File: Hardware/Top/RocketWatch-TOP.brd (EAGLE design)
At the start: 160 x 100 mm, 0 parts

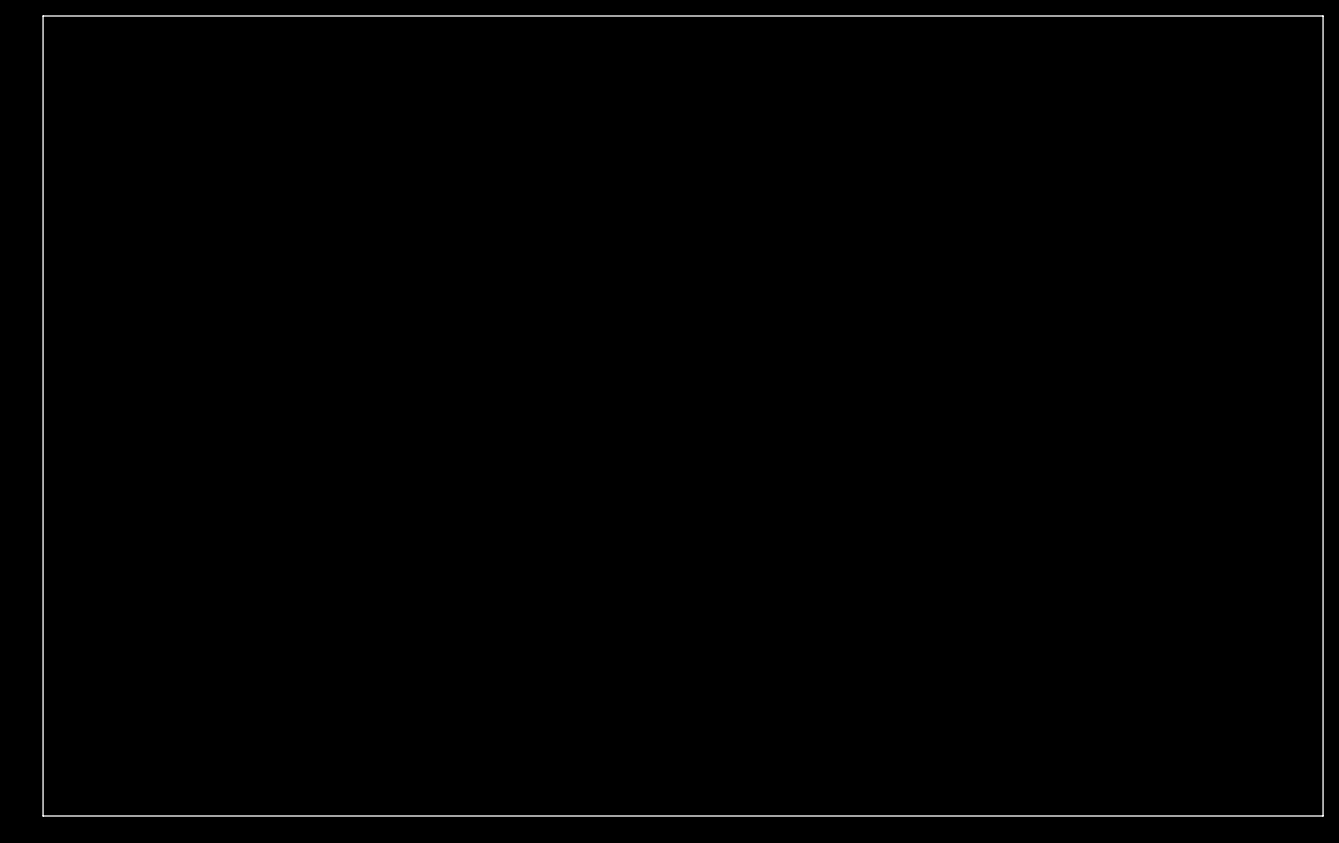
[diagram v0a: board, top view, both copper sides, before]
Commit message: updates to the board and schematic (added microcontroller, power management, OLED, Buttons, and a few other components)
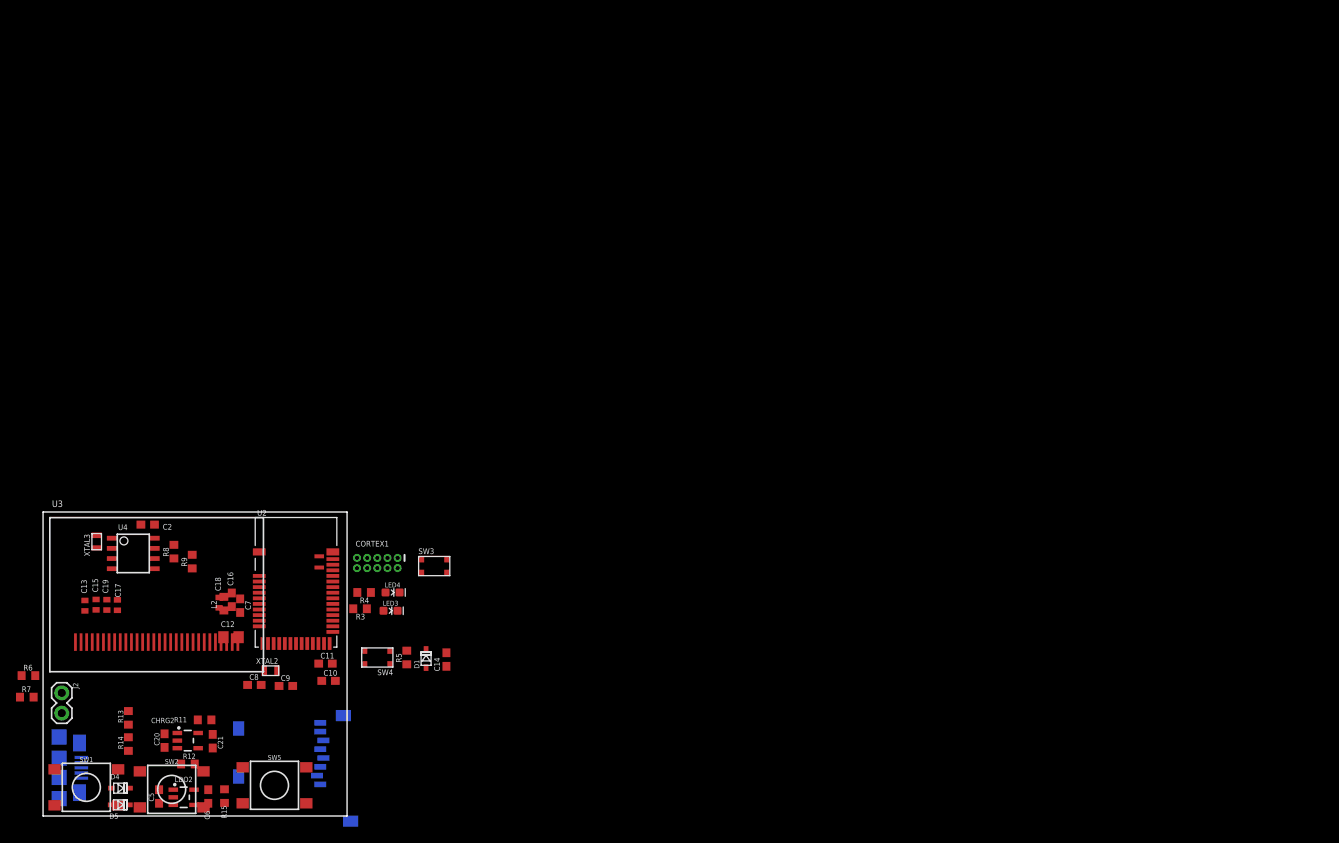
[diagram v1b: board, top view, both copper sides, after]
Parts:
- added C10, C11: 300p, LinnesLab-Passives:C0603
- added C12: 10u, LinnesLab-Passives:C0805
- added C13, C15, C17, C18, C19: 2.2uF, LinnesLab-Passives:C0402
- added C14: 100n, LinnesLab-Passives:C0603
- added C16: 10uF, LinnesLab-Passives:C0603
- added C2, C5, C6, C7: 1u, LinnesLab-Passives:C0603
- added C20, C21: 4.7u, LinnesLab-Passives:C0603
- added C8, C9: (no value), LinnesLab-Passives:C0603
- added CHRG2: MCP73831, LinnesLab-Power:SOT23-5
- added CORTEX1: CORTEX_DEBUG_PTH, LinnesLab-Connectors:2X5-PTH-1.27MM
- added D1, D4, D5: (no value), LinnesLab-DiscreteSemi:USC
- added J2: (no value), LinnesLab-Connectors:1X02
- added L2: 10u, LinnesLab-Passives:L0603
- added LDO2: MIC5504, LinnesLab-Power:SOT23-5
- added LED3: RED, LinnesLab-LED:LED-0603
- added LED4: BLUE, LinnesLab-LED:LED-0603
- added R11: (no value), LinnesLab-Passives:R0603
- added R12, R13, R14, R15: 100k, LinnesLab-Passives:R0603
- added R3, R4: 1k, LinnesLab-Passives:R0603
- added R5, R6, R8, R9: 10k, LinnesLab-Passives:R0603
- added R7: 390k, LinnesLab-Passives:R0603
- added SD2: (no value), LinnesLab-Connectors:MICROSD
- added SW1, SW2, SW5: SWITCH.MOM, LinnesLab-Switches:TACTILE_SWITCH_SMD_6.2MM_TALL
- added SW3, SW4: (no value), LinnesLab-Switches:BUTTON-GULLWING
- added U2: NRF52832_MODULE_MDBT42, LinnesLab-Microcontrollers:BLE_MODULE_RAYTAC_MDBT42
- added U3: (no value), LinnesLab-Displays:UG-2864HSWEG01_0.96IN_NO-WRAPAROUND
- added U4: PCF8523, LinnesLab-Clocks:SO8
- added USB2: USB.MICRO-BIGGERPADS, LinnesLab-Connectors:USB-MICRO-01.BIGGERPADS
- added XTAL2: 32.768kHz, LinnesLab-Clocks:2-SMD.NOLEAD.2.0MMTO1.2MM
- added XTAL3: 32.7680kHz, LinnesLab-Clocks:2-SMD.NOLEAD.2.0MMTO1.2MM
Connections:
- new net 3.3V: C12.2, C17.2, C19.2, C2.1, C6.1, CORTEX1.1, D1.-, LDO2.5, R15.2, R5.2, R8.2, R9.2, SD2.4, U2.11, U3.6, U3.9, U4.8
- new net BATT: R13.1, R14.2
- new net CD1: SD2.CD1
- new net CD2: SD2.CD2
- new net CHRG.STAT: CHRG2.1, R12.1
- new net CS.OLED: U3.13
- new net DC.OLED: U3.15
- new net DFU: SW3.3, U2.34
- new net DTR: C14.1
- new net FRST: U2.38
- new net GND: C10.2, C11.2, C12.1, C16.1, C17.1, C18.1, C19.1, C2.2, C20.2, C21.1, C5.1, C6.2, C7.2, C8.1, C9.2, CHRG2.2, CORTEX1.3, CORTEX1.5, CORTEX1.7, CORTEX1.9, J2.1, LDO2.2, LED3.C, LED4.C, R11.1, R14.1, R15.1, R6.1, R7.2, SD2.6, SD2.MT1, SD2.MT2, SW3.1, SW4.3, U2.1, U2.12, U2.24, U2.39, U3.1, U3.10, U3.12, U3.29, U3.30, U3.8, U4.4, USB2.5
- new net LED1: R3.2, U2.31
- new net LED2: R4.2, U2.33
- new net MISO: SD2.7, U2.28
- new net MOSI: SD2.3, U2.27, U3.19
- new net N$1: R6.2, U3.11
- new net N$10: LED4.A, R4.1
- new net N$11: L2.1, U2.10
- new net N$12: C7.1, L2.2, U2.9
- new net N$13: C16.2, U3.28
- new net N$14: CORTEX1.8
- new net N$15: C18.2, U3.27
- new net N$17: CHRG2.5, R11.2
- new net N$19: U4.2, XTAL3.P$1
- new net N$2: R7.1, U3.26
- new net N$20: U4.1, XTAL3.P$2
- new net N$3: C13.2, U3.2
- new net N$4: C8.2, U2.13, XTAL2.P$1
- new net N$5: C13.1, U3.3
- new net N$6: C9.1, U2.14, XTAL2.P$2
- new net N$7: C15.2, U3.4
- new net N$8: C15.1, U3.5
- new net N$9: LED3.A, R3.1
- new net P0.09/NFC1: C11.1, U2.22
- new net P0.10/NFC2: C10.1, U2.23
- new net RESET: C14.2, CORTEX1.10, D1.+, R5.1, SW4.1, U2.35
- new net RESET.OLED: U3.14
- new net RXD: U2.21
- new net SCK: SD2.5, U2.26, U3.18
- new net SCL: R8.1, U2.3, U4.6
- new net SD.CS: SD2.2
- new net SDA: R9.1, U2.2, U4.5
- new net SWCLK: CORTEX1.4, U2.36
- new net SWDIO: CORTEX1.2, U2.37
- new net SWO: CORTEX1.6, U2.32
- new net TXD: U2.19
- new net USB+: USB2.3
- new net USB-: USB2.2
- new net VBATT: U4.3
- new net VIN: C21.2, C5.2, CHRG2.4, D4.-, D5.-, LDO2.1, LDO2.3, R12.2
- new net VLIPO: C20.1, CHRG2.3, D4.+, J2.2, R13.2
- new net V_USB: D5.+, USB2.1
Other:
- board size 160 x 100 mm -> 38 x 38 mm
